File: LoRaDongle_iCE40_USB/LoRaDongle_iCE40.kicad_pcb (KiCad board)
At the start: 4 copper layers, 110 x 45 mm, 128 parts, among them IC1 93LC56BT-I_OT, IC2 ICE40UP5K-UWG30ITR1K, IC3 N25Q032A13ESC40F, J1 USB_A, J2 Conn_01x08, J3 Conn_02x02_Top_Bottom, J4 Jumper, J5 142-0701-801, J6 Conn_01x06, J7 Jumper_NC_Small, J8 Jumper, J9 Conn_02x02_Top_Bottom, SW1 SW_Push, U1 RP550K001A-TR, U2 FT232H, U3 SX1261IMLTRT, U4 SKY13587-378LF, X1 ECS-2520MV-500-BL-TR, Y1 Crystal_GND24_Small, Y2 Crystal_GND24

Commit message: switched relative libraries
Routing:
- net /SPI_MISO: track 72.0 -> 65.2 mm, vias 1 -> 2
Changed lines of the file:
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@@
   (segment (start 143.0575 103.2525) (end 143.0575 109.8025) (width 0.3) (layer "In1.Cu") (net 61))
   (segment (start 143.0575 109.8025) (end 141.01 111.85) (width 0.3) (layer "In1.Cu") (net 61))
-  (segment (start 142.060736 105.687) (end 144.878 105.687) (width 0.3) (layer "F.Cu") (net 62))
+  (segment (start 142.060736 105.687) (end 142.073 105.687) (width 0.3) (layer "F.Cu") (net 62))
   (segment (start 138.72 117.4) (end 134.97 113.65) (width 0.3) (layer "F.Cu") (net 62))
-  (segment (start 146 96.45) (end 140.6 101.85) (width 0.3) (layer "F.Cu") (net 62))
+  (segment (start 146 96.45) (end 141.35 101.1) (width 0.3) (layer "F.Cu") (net 62))
   (segment (start 131.73 107.16) (end 131.73 104.53) (width 0.3) (layer "F.Cu") (net 62))
   (segment (start 155.38 117.4) (end 138.72 117.4) (width 0.3) (layer "F.Cu") (net 62))
+  (segment (start 141.35 101.1) (end 140.6 101.85) (width 0.3) (layer "F.Cu") (net 62))
   (segment (start 140.6 104.226264) (end 142.060736 105.687) (width 0.3) (layer "F.Cu") (net 62))
   (segment (start 158.36 114.42) (end 155.38 117.4) (width 0.3) (layer "F.Cu") (net 62))
   (segment (start 131.75 101.6625) (end 131.75 104.51) (width 0.3) (layer "F.Cu") (net 62))
   (segment (start 140.6 101.85) (end 140.6 104.226264) (width 0.3) (layer "F.Cu") (net 62))
+  (segment (start 142.073 105.687) (end 144.878 105.687) (width 0.3) (layer "F.Cu") (net 62))
   (segment (start 134.97 110.4) (end 131.73 107.16) (width 0.3) (layer "F.Cu") (net 62))
   (segment (start 131.75 104.51) (end 131.73 104.53) (width 0.3) (layer "F.Cu") (net 62))
   (segment (start 134.97 113.65) (end 134.97 110.4) (width 0.3) (layer "F.Cu") (net 62))
+  (via (at 142.073 105.687) (size 0.8) (drill 0.4) (layers "F.Cu" "B.Cu") (net 62))
   (via (at 131.73 104.53) (size 0.8) (drill 0.4) (layers "F.Cu" "B.Cu") (net 62))
-  (segment (start 132.3 103.96) (end 131.73 104.53) (width 0.3) (layer "B.Cu") (net 62))
-  (segment (start 143.03 99.42) (end 146 96.45) (width 0.3) (layer "B.Cu") (net 62))
-  (segment (start 132.31 103.96) (end 132.3 103.96) (width 0.3) (layer "B.Cu") (net 62))
-  (segment (start 132.31 103.96) (end 136.85 99.42) (width 0.3) (layer "B.Cu") (net 62))
-  (segment (start 136.85 99.42) (end 143.03 99.42) (width 0.3) (layer "B.Cu") (net 62))
+  (segment (start 131.73 104.53) (end 131.759511 104.559511) (width 0.3) (layer "B.Cu") (net 62))
+  (segment (start 140.945511 104.559511) (end 142.073 105.687) (width 0.3) (layer "B.Cu") (net 62))
+  (segment (start 131.759511 104.559511) (end 140.945511 104.559511) (width 0.3) (layer "B.Cu") (net 62))
   (segment (start 144.878 106.957) (end 143.043 106.957) (width 0.3) (layer "F.Cu") (net 63))
   (segment (start 143.043 106.957) (end 143 107) (width 0.3) (layer "F.Cu") (net 63))

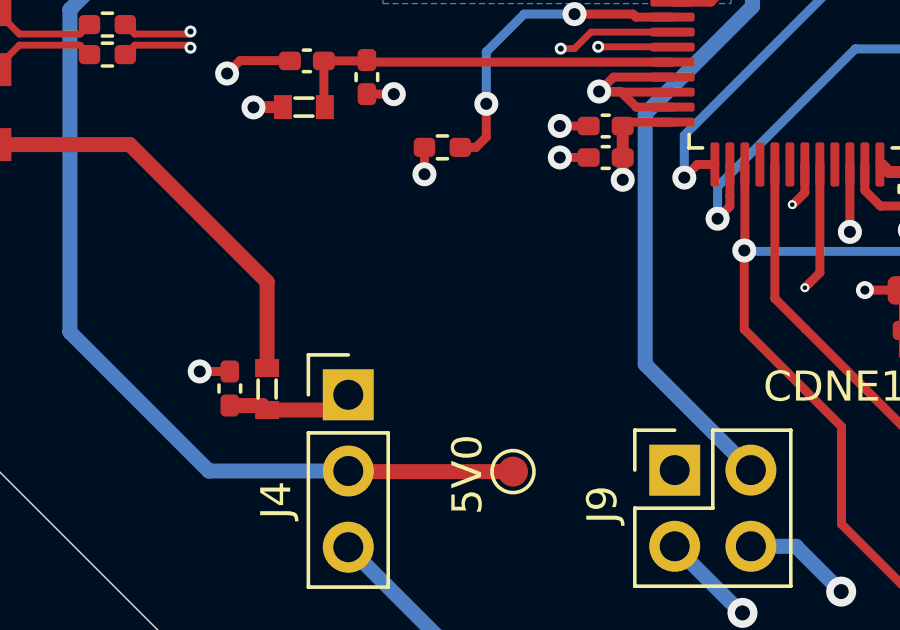
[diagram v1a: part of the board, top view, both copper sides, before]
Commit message: update vias and text on schematic
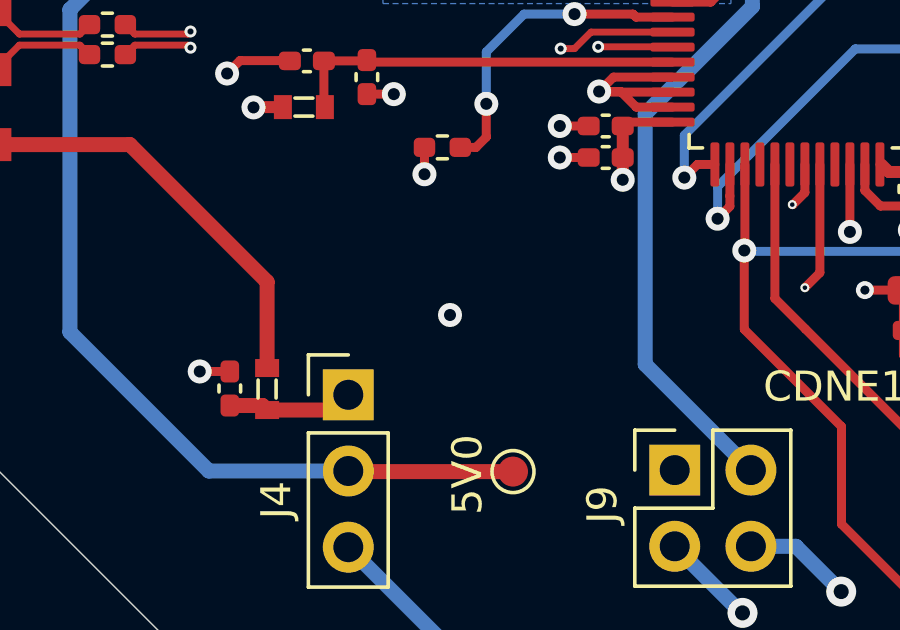
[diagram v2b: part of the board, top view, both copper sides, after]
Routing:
- net GND: vias 79 -> 80
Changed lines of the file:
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@@
   (via (at 141.59 96.85) (size 0.8) (drill 0.4) (layers "F.Cu" "B.Cu") (net 1))
   (via (at 178.96 102) (size 1) (drill 0.5) (layers "F.Cu" "B.Cu") (net 1))
+  (via (at 121.92 106.68) (size 0.8) (drill 0.4) (layers "F.Cu" "B.Cu") (free) (net 1))
   (via (at 200.22 82.72) (size 1) (drill 0.5) (layers "F.Cu" "B.Cu") (net 1))
   (via (at 207.865 109.715) (size 1) (drill 0.5) (layers "F.Cu" "B.Cu") (net 1))

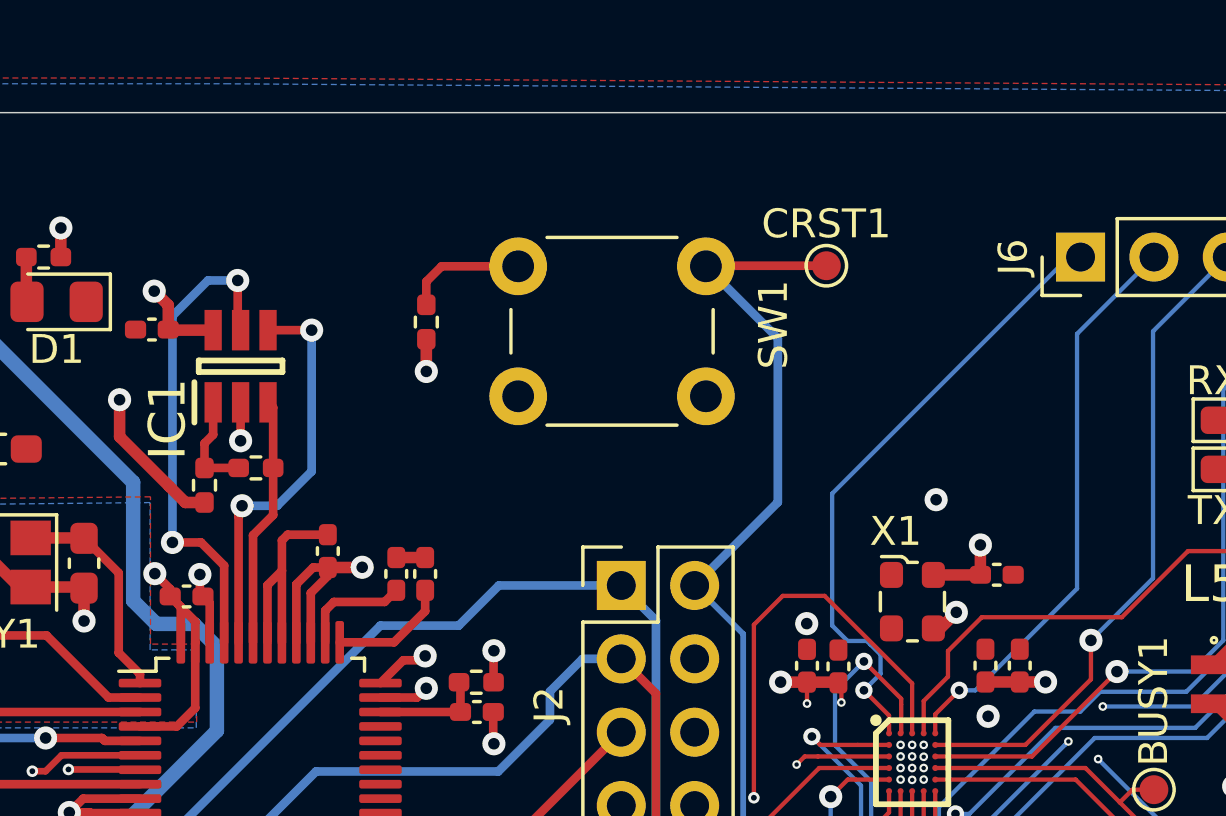
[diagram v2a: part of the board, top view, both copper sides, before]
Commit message: added usb flash testpoints & jumper for fpga oscillator
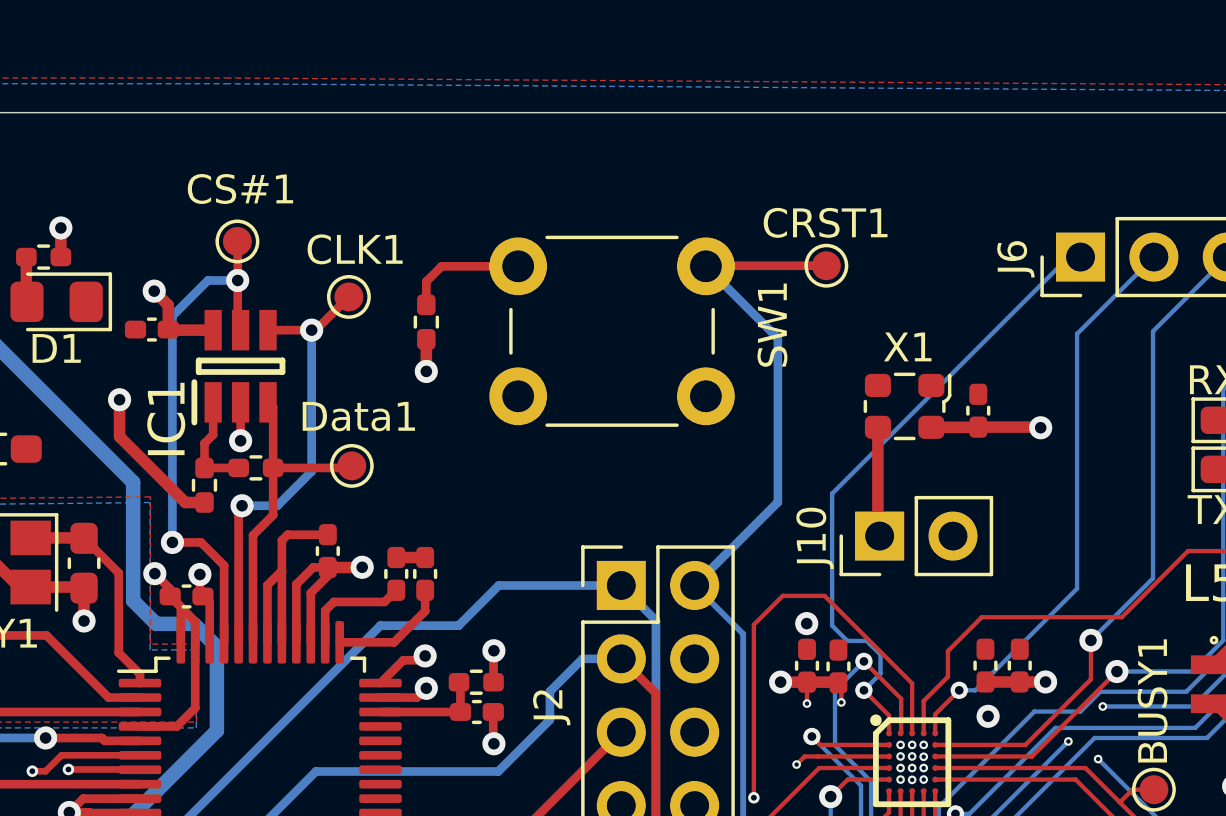
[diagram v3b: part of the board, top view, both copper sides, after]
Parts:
- added CLK1: CLK, TestPoint:TestPoint_Pad_D1.0mm, F.Cu at (136.6, 81.4)
- added CS#1: CS#, TestPoint:TestPoint_Pad_D1.0mm, F.Cu at (132.7, 79.5)
- added Data1: Data, TestPoint:TestPoint_Pad_D1.0mm, F.Cu at (136.7, 87.2)
- added J10: Jumper_2_Open, Connector_PinHeader_2.54mm:PinHeader_1x02_P2.54mm_Vertical, F.Cu at (154.9, 89.7)
- R12: value R -> 4K7
- moved X1 6.77 mm to (155.8, 85.2), turned to -90 degrees
- moved C23 5.72 mm to (158.4, 85.3), turned to -90 degrees
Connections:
- X1 pad 3: /ice40up5k_circuit/iCE_CLK -> Net-(J10-Pad1)
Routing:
- net Net-(J10-Pad1): track 0.00 -> 3.79 mm
- net /USB_Interface/DATA: track 8.67 -> 11.4 mm
- net /USB_Interface/CLK: track 14.1 -> 15.8 mm
- net /ice40up5k_circuit/iCE_CLK: track 6.25 -> 7.82 mm, vias 2 -> 1
- net /USB_Interface/CS#: track 17.1 -> 18.5 mm
- net 3V3: track 52.1 -> 53.3 mm
- net GND: vias 80 -> 79

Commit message: updating silkscreen
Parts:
- renumbered SW1 to RESET
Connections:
- U3 pad 6: /RF Circuitry/DIO3 -> unconnected-(U3-Pad6)
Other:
- board text added: "!SS SPI FLASH"
- board text added: "CONFIG FPGA"
- board text added: "EXTERNAL"
- board text added: "FB1"
- board text added: "FB2"
- board text added: "FB3"
- board text added: "FPGA POWER"
- board text added: "ON:"
- board text added: "PROGRAM FLASH"
- board text added: "PWR SELECT"
- board text added: "SPI CONFIG"
- board text added: "USB"

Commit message: completed silkscreen
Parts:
- added G1: LOGO, Logo:LoRaDongleLogo, F.Cu at (193.3, 78.5)
- added G2: LOGO, Logo:rev1.0, F.Cu at (201.1, 116.0)
- added G3: LOGO, Logo:mark_njoroge, B.Cu at (189.6, 114.2)
- added REF**: OSHW-Symbol_6.7x6mm_SilkScreen, Symbol:OSHW-Symbol_6.7x6mm_SilkScreen, B.Cu at (194.2, 104.0)
- added REF**: KiCad-Logo2_5mm_SilkScreen, Symbol:KiCad-Logo2_5mm_SilkScreen, B.Cu at (178.3, 104.0)
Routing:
- net GND: track 208.1 -> 210.8 mm, vias 79 -> 80
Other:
- board text added: "+"
- board text added: "."
- board text added: "EXTRA PINOUT"
- board text added: "FLASH"
- board text added: "FPGA"
- board text added: "FT232 BREAKOUT CONNECTOR"
- board text added: "GND"
- board text added: "OFF:"
- board text added: "OSC"
- board text added: "RADIO POWER"
- board text added: "SELECT FLASH"
- board text added: "Vin"
- board text removed: "!SS SPI FLASH"
- board text removed: "CONFIG FPGA"
- board text removed: "PROGRAM FLASH"
